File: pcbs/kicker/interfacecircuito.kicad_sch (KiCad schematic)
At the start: 70 parts, among them J1 XT30PW-F, J2 12V, J3 3.3V, J4 BOOST_BOARD, J5 Conn_02x08_Odd_Even, J6 Conn_01x03, Q1 IRFB3077, Q2 IRFB3077, Q3 BC338, U2 IR2101, U3 PC817, U4 LM358, U5 LM324, U6 LM324

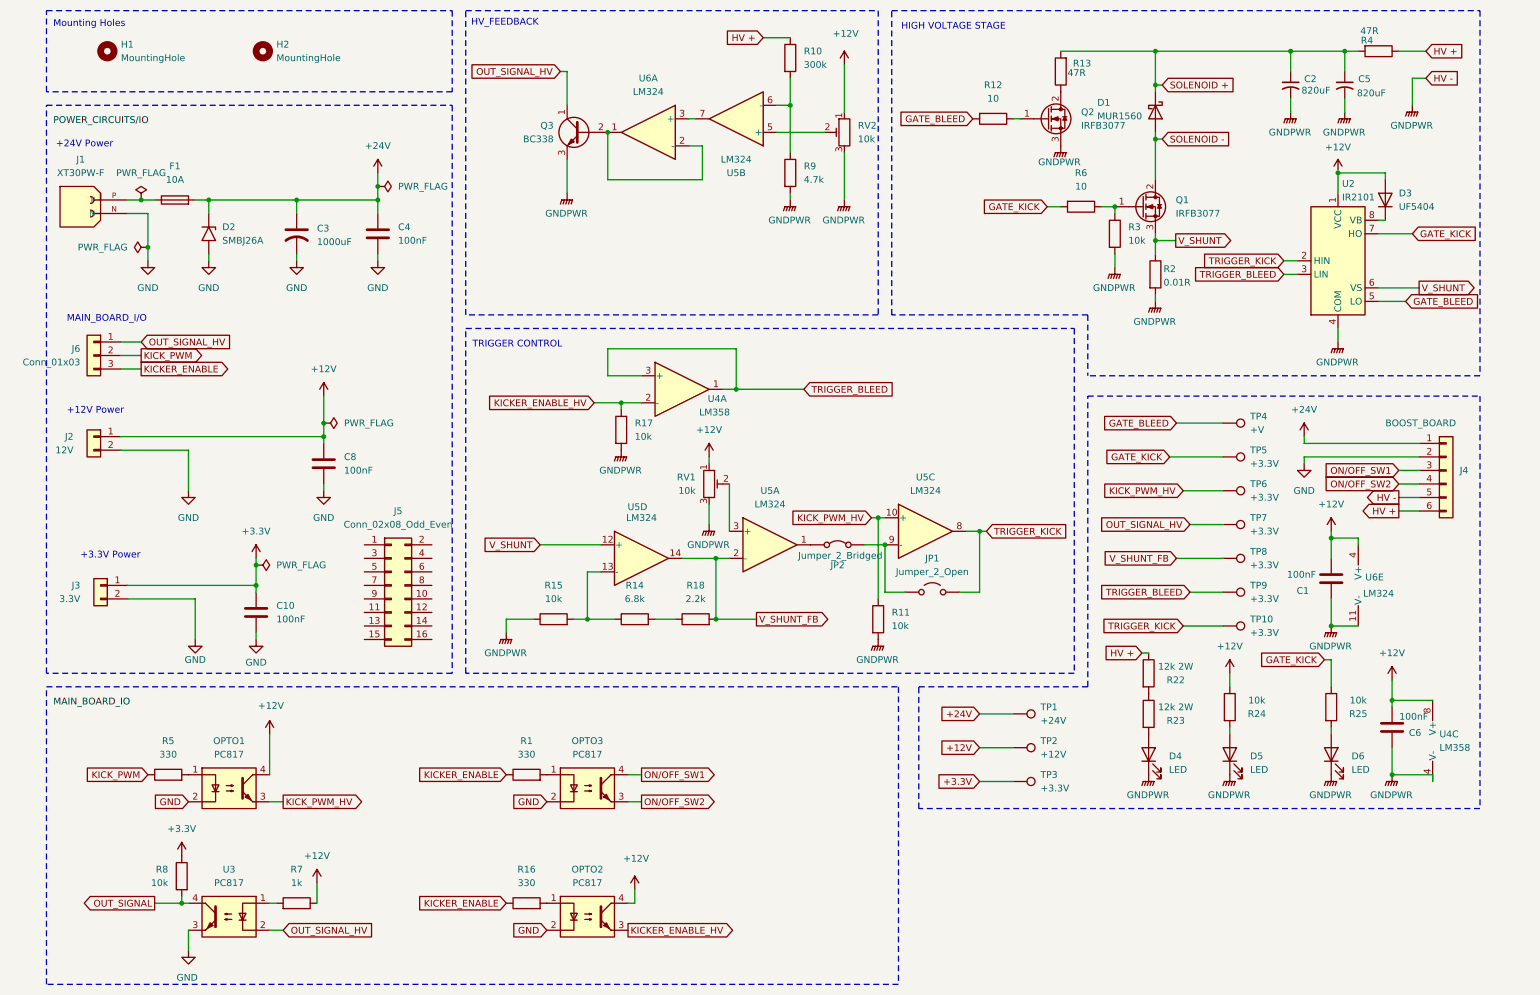
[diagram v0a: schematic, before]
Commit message: Roteamento das trilhas & Footprints
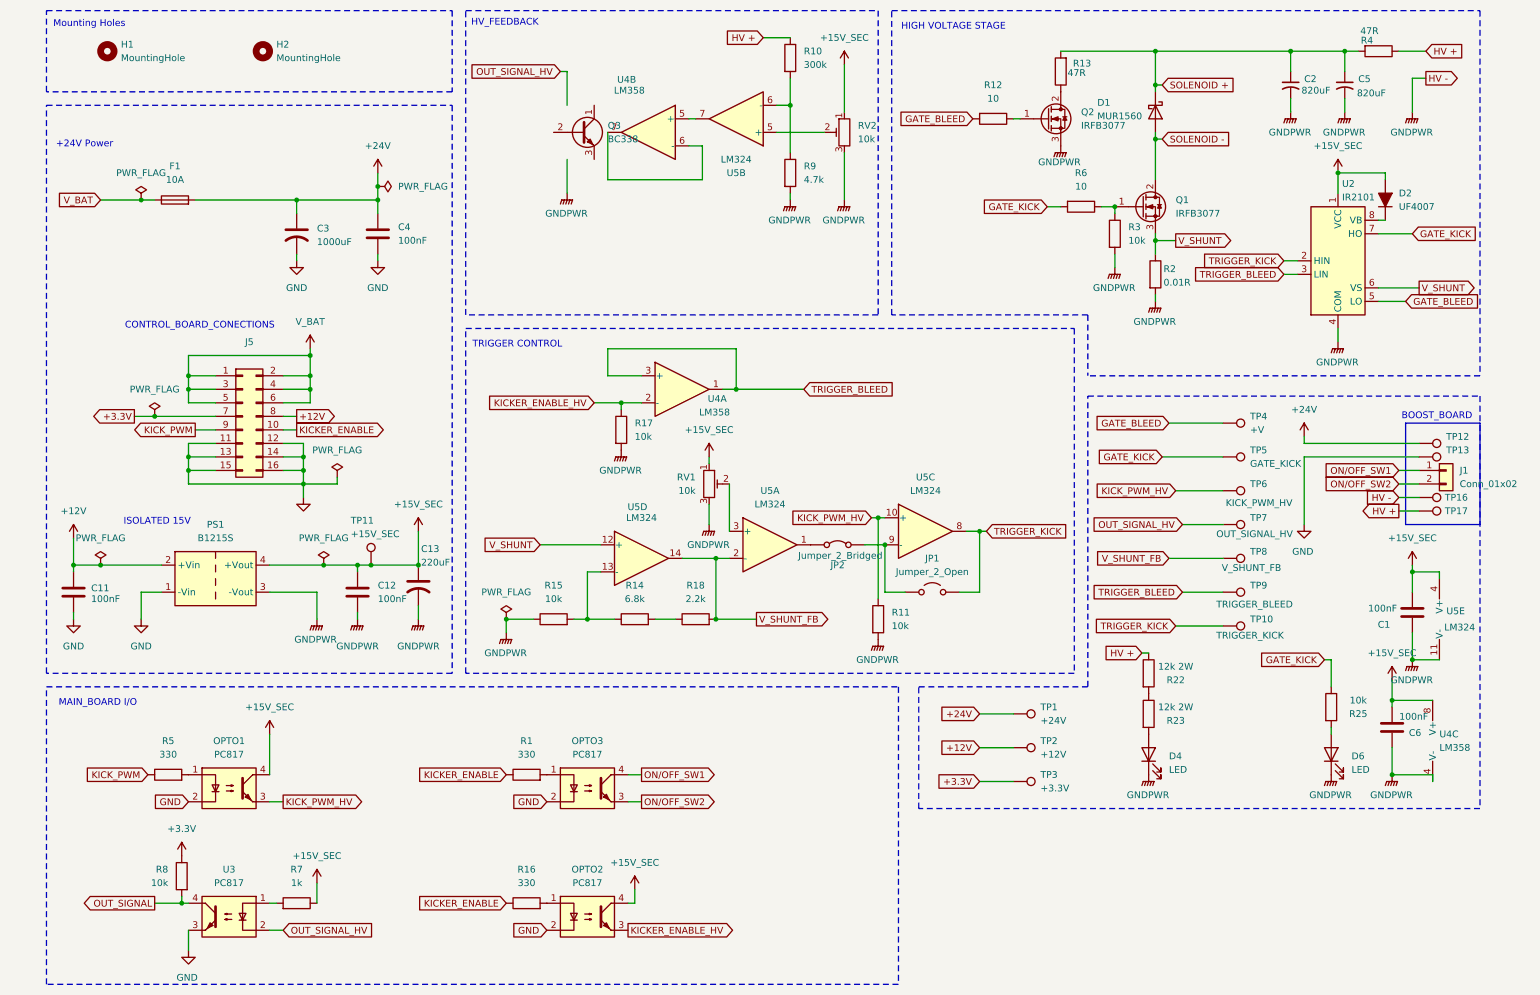
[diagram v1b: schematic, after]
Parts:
- removed C10, C8: 100nF, Capacitor_SMD:C_0805_2012Metric_Pad1.18x1.45mm_HandSolder, symbol Device:C
- removed D2: SMBJ26A, Diode_SMD:D_SMB, symbol Diode:SMAJ26A
- removed D3: UF5404, Diode_THT:D_DO-201AD_P15.24mm_Horizontal, symbol Diode:UF5404
- removed D5: LED, symbol Device:LED
- removed J1: XT30PW-F, oxebots:AMASS_XT30PW-M, symbol oxebots:XT30PW-F
- removed J2: 12V, Connector_JST:JST_PH_S2B-PH-K_1x02_P2.00mm_Horizontal, symbol Connector_Generic:Conn_01x02
- removed J3: 3.3V, Connector_JST:JST_PH_S2B-PH-K_1x02_P2.00mm_Horizontal, symbol Connector_Generic:Conn_01x02
- removed J4: BOOST_BOARD, symbol Connector_Generic:Conn_01x06
- removed J6: Conn_01x03, symbol Connector_Generic:Conn_01x03
- removed R24: 10k, Resistor_SMD:R_2512_6332Metric_Pad1.40x3.35mm_HandSolder, symbol Device:R
- removed unit 1 of U6
- added C11, C12: 100nF, Capacitor_THT:C_Disc_D5.0mm_W2.5mm_P2.50mm, symbol Device:C
- added C13: 220uF, Capacitor_THT:CP_Radial_D8.0mm_P5.00mm, symbol Device:C_US
- added D2: UF4007, PCM_Diode_THT_AKL:D_DO-41_SOD81_P10.16mm_Horizontal, symbol PCM_Diode_AKL:UF4007
- added J1: Conn_01x02, Connector_PinHeader_1.00mm:PinHeader_1x02_P1.00mm_Vertical, symbol Connector_Generic:Conn_01x02
- added PS1: B1215S, oxebots:DC-DC_Converter_BxxxxS_1W, symbol oxebots:Converter_DC-DC_BxxxxS
- added TP11: +15V_SEC, TestPoint:TestPoint_Pad_D1.5mm, symbol Connector:TestPoint
- added TP12: V+, TestPoint:TestPoint_Plated_Hole_D2.0mm, symbol Connector:TestPoint
- added TP13: GND, TestPoint:TestPoint_Plated_Hole_D2.0mm, symbol Connector:TestPoint
- added TP16: HV-, TestPoint:TestPoint_Plated_Hole_D2.0mm, symbol Connector:TestPoint
- added TP17: HV+, TestPoint:TestPoint_Plated_Hole_D2.0mm, symbol Connector:TestPoint
- added unit 2 of U4
- C1, C6: footprint (none) -> Capacitor_THT:C_Disc_D5.0mm_W2.5mm_P2.50mm
- C2, C5: footprint (none) -> Capacitor_THT:C_Radial_D18.0mm_H35.5mm_P7.50mm
- C4: footprint Capacitor_SMD:C_0805_2012Metric_Pad1.18x1.45mm_HandSolder -> Capacitor_THT:C_Disc_D5.0mm_W2.5mm_P2.50mm
- D1: footprint (none) -> Package_TO_SOT_THT:TO-220-2_Vertical
- D4, D6: footprint (none) -> LED_SMD:LED_0805_2012Metric_Pad1.15x1.40mm_HandSolder
- JP1: footprint (none) -> Jumper:SolderJumper-2_P1.3mm_Open_RoundedPad1.0x1.5mm
- JP2: footprint (none) -> Jumper:SolderJumper-2_P1.3mm_Bridged_RoundedPad1.0x1.5mm
- Q1, Q2: footprint (none) -> Package_TO_SOT_THT:TO-220-3_Vertical
- R1, R11, R12, R14, R15, R16, R17, R18, R3, R5, R6, R7, R8, R9: footprint (none) -> Resistor_THT:R_Axial_DIN0207_L6.3mm_D2.5mm_P10.16mm_Horizontal
- R10: footprint (none) -> Resistor_THT:R_Axial_DIN0411_L9.9mm_D3.6mm_P15.24mm_Horizontal
- R13, R4: footprint (none) -> PCM_Resistor_THT_AKL:R_Axial_Power_L25.0mm_W9.0mm_P30.48mm
- R2: footprint (none) -> PCM_Resistor_THT_AKL:R_Axial_DIN0516_L15.5mm_D5.0mm_P20.32mm_Horizontal
- R22, R23: footprint Resistor_SMD:R_2512_6332Metric_Pad1.40x3.35mm_HandSolder -> Resistor_THT:R_Axial_DIN0617_L17.0mm_D6.0mm_P20.32mm_Horizontal
- R25: footprint Resistor_SMD:R_2512_6332Metric_Pad1.40x3.35mm_HandSolder -> Resistor_THT:R_Axial_DIN0207_L6.3mm_D2.5mm_P10.16mm_Horizontal
- RV1, RV2: footprint (none) -> Potentiometer_THT:Potentiometer_Bourns_3296W_Vertical
- TP10: value +3.3V -> TRIGGER_KICK
- TP5: value +3.3V -> GATE_KICK
- TP6: value +3.3V -> KICK_PWM_HV
- TP7: value +3.3V -> OUT_SIGNAL_HV
- TP8: value +3.3V -> V_SHUNT_FB
- TP9: value +3.3V -> TRIGGER_BLEED
- U2, U4: footprint (none) -> Package_SO:SOIC-8_3.9x4.9mm_P1.27mm
- U5: renamed from U6; footprint (none) -> Package_SO:SOIC-14_3.9x8.7mm_P1.27mm
- U5: footprint (none) -> Package_SO:SOIC-14_3.9x8.7mm_P1.27mm
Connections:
- net +12V: now also J5.8 (Pin_8), C11.1, PS1.2 (+Vin); no longer C1.1, C6.1, OPTO1.4, OPTO2.4, R7.1, RV1.1, RV2.1, U2.1 (VCC), U4.8 (V+), U5.4 (V+)
- net +24V: now also TP12.1
- net +3.3V: now also J5.7 (Pin_7)
- net GND: now also J5.11 (Pin_11), J5.12 (Pin_12), J5.13 (Pin_13), J5.14 (Pin_14), J5.15 (Pin_15), J5.16 (Pin_16), C11.2, PS1.1 (-Vin), TP13.1
- net GNDPWR: now also C12.2, C13.2, PS1.3 (-Vout), TP16.1; no longer Q3.3 (E)
- net HV +: now also TP17.1
- net KICKER_ENABLE: now also J5.10 (Pin_10)
- net KICK_PWM: now also J5.9 (Pin_9)
- net ON/OFF_SW1: now also J1.1 (Pin_1)
- net ON/OFF_SW2: now also J1.2 (Pin_2)
- net OUT_SIGNAL_HV: no longer Q3.1 (C)
- net at U2.8 (VB): now also D2.1 (K)
- net V_BAT: now reaches F1.1
- net V_BAT: now also J5.1 (Pin_1), J5.2 (Pin_2), J5.3 (Pin_3), J5.4 (Pin_4), J5.5 (Pin_5), J5.6 (Pin_6)
- net at U5.7: now also U4.5 (+)
- new net: U4.6 (-), U4.7
- new net +15V_SEC: C1.1, C12.1, C13.1, C6.1, D2.2 (A), OPTO1.4, OPTO2.4, PS1.4 (+Vout), R7.1, RV1.1, RV2.1, TP11.1, U2.1 (VCC), U4.8 (V+), U5.4 (V+)
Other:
- note added: "BOOST_BOARD"
- note added: "CONTROL_BOARD_CONECTIONS"
- note added: "ISOLATED 15V"
- note added: "MAIN_BOARD I/O"
- note removed: "+12V Power"
- note removed: "+3.3V Power"
- note removed: "MAIN_BOARD_I/O"
- moved on the sheet: C1, J5, Q3, U5E

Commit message: Resolução de Warnings do esquemático, substituição de conectores on/off e conector de solenoide
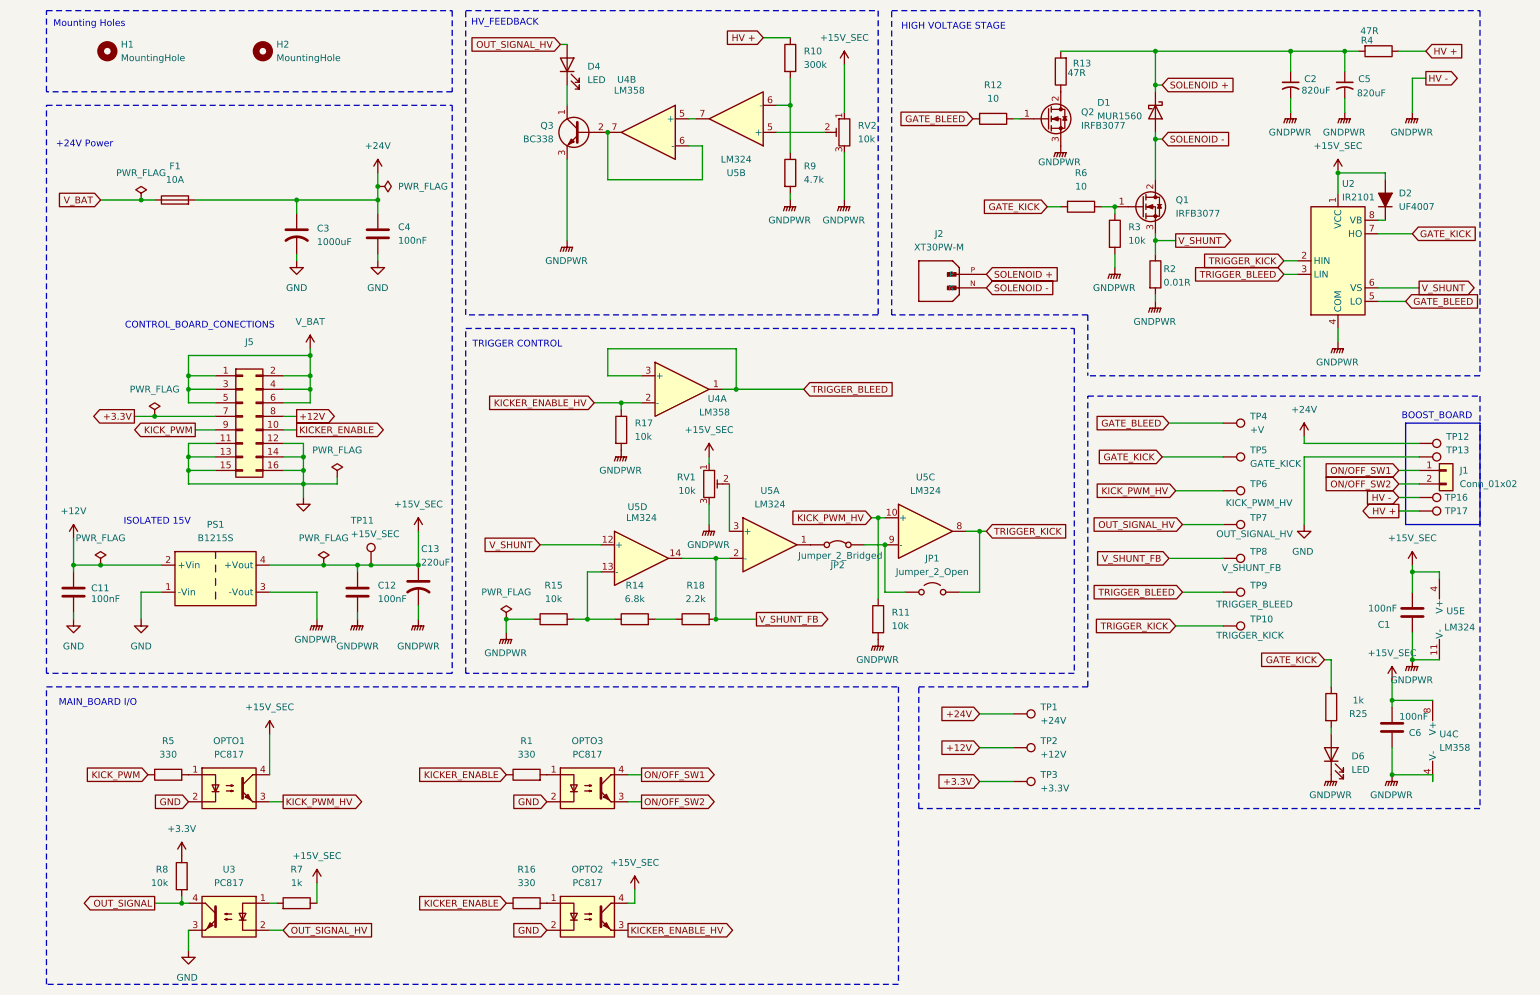
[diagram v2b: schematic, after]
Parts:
- removed R22, R23: 12k 2W, Resistor_THT:R_Axial_DIN0617_L17.0mm_D6.0mm_P20.32mm_Horizontal, symbol Device:R
- added J2: XT30PW-M, oxebots:AMASS_XT30PW-M, symbol oxebots:XT30PW-M
- D4, D6: footprint LED_SMD:LED_0805_2012Metric_Pad1.15x1.40mm_HandSolder -> LED_THT:LED_D5.0mm
- J1: footprint Connector_PinHeader_1.00mm:PinHeader_1x02_P1.00mm_Vertical -> Connector_JST:JST_EH_B2B-EH-A_1x02_P2.50mm_Vertical
- R25: value 10k -> 1k
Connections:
- net GNDPWR: now also Q3.3 (E); no longer D4.1 (K)
- net OUT_SIGNAL_HV: now also D4.2 (A)
- net SOLENOID +: now also J2.P
- net SOLENOID -: now also J2.N
- net at Q3.1 (C): now also D4.1 (K)
- net at Q3.2 (B): now also U4.6 (-), U4.7
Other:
- moved on the sheet: Q3

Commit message: Resolução de EDR Mudança nas trilhas de 24V mudança do footprint dos capacitores bulk
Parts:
- C2, C5: footprint Capacitor_THT:C_Radial_D18.0mm_H35.5mm_P7.50mm -> Capacitor_THT:CP_Radial_D30.0mm_P10.00mm_SnapIn
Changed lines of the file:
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@@
 	)
 	(junction
-		(at 66.04 118.11)
+		(at 222.25 45.72)
 		(diameter 0)
 		(color 0 0 0 0)
@@
 	(wire
 		(pts
+			(xy 222.25 45.72) (xy 231.14 45.72)
+		)
+		(stroke
+			(width 0)
+			(type default)
+		)
+	)
+	(wire
+		(pts
 			(xy 62.23 95.25) (xy 58.42 95.25)
 		)
@@
 	(wire
 		(pts
-			(xy 66.04 118.11) (xy 74.93 118.11)
+			(xy 55.88 118.11) (xy 74.93 118.11)
 		)
 		(stroke
@@
 	(wire
 		(pts
-			(xy 55.88 118.11) (xy 66.04 118.11)
-		)
-		(stroke
-			(width 0)
-			(type default)
-		)
-	)
-	(wire
-		(pts
 			(xy 274.32 157.48) (xy 266.7 157.48)
 		)
@@
 			)
 		)
-		(property "Footprint" "Capacitor_THT:C_Radial_D18.0mm_H35.5mm_P7.50mm"
+		(property "Footprint" "Capacitor_THT:CP_Radial_D30.0mm_P10.00mm_SnapIn"
 			(at 257.81 27.94 0)
 			(hide yes)
@@
 			)
 		)
-		(property "Footprint" "Capacitor_THT:C_Radial_D18.0mm_H35.5mm_P7.50mm"
+		(property "Footprint" "Capacitor_THT:CP_Radial_D30.0mm_P10.00mm_SnapIn"
 			(at 247.65 27.94 0)
 			(hide yes)
@@
 	)
 	(symbol
+		(lib_id "power:PWR_FLAG")
+		(at 222.25 21.59 0)
+		(unit 1)
+		(body_style 1)
+		(exclude_from_sim no)
+		(in_bom yes)
+		(on_board yes)
+		(in_pos_files yes)
+		(dnp no)
+		(fields_autoplaced yes)
+		(property "Reference" "#FLG010"
+			(at 222.25 19.685 0)
+			(hide yes)
+			(show_name no)
+			(do_not_autoplace no)
+			(effects
+				(font
+					(size 1.27 1.27)
+				)
+			)
+		)
+		(property "Value" "PWR_FLAG"
+			(at 222.25 16.51 0)
+			(show_name no)
+			(do_not_autoplace no)
+			(effects
+				(font
+					(size 1.27 1.27)
+				)
+			)
+		)
+		(property "Footprint" ""
+			(at 222.25 21.59 0)
+			(hide yes)
+			(show_name no)
+			(do_not_autoplace no)
+			(effects
+				(font
+					(size 1.27 1.27)
+				)
+			)
+		)
+		(property "Datasheet" "~"
+			(at 222.25 21.59 0)
+			(hide yes)
+			(show_name no)
+			(do_not_autoplace no)
+			(effects
+				(font
+					(size 1.27 1.27)
+				)
+			)
+		)
+		(property "Description" "Special symbol for telling ERC where power comes from"
+			(at 222.25 21.59 0)
+			(hide yes)
+			(show_name no)
+			(do_not_autoplace no)
+			(effects
+				(font
+					(size 1.27 1.27)
+				)
+			)
+		)
+		(pin "1"
+		)
+		(instances
+			(project "interfacecircuito"
+				(path "/21d6ebf1-8438-4874-a5b6-238c3ba91f04"
+					(reference "#FLG010")
+					(unit 1)
+				)
+			)
+		)
+	)
+	(symbol
 		(lib_id "Connector:TestPoint")
 		(at 234.95 129.54 270)
@@
 	)
 	(symbol
-		(lib_id "power:PWR_FLAG")
-		(at 66.04 118.11 0)
-		(unit 1)
-		(body_style 1)
-		(exclude_from_sim no)
-		(in_bom yes)
-		(on_board yes)
-		(in_pos_files yes)
-		(dnp no)
-		(fields_autoplaced yes)
-		(property "Reference" "#FLG07"
-			(at 66.04 116.205 0)
-			(hide yes)
-			(show_name no)
-			(do_not_autoplace no)
-			(effects
-				(font
-					(size 1.27 1.27)
-				)
-			)
-		)
-		(property "Value" "PWR_FLAG"
-			(at 66.04 113.03 0)
-			(show_name no)
-			(do_not_autoplace no)
-			(effects
-				(font
-					(size 1.27 1.27)
-				)
-			)
-		)
-		(property "Footprint" ""
-			(at 66.04 118.11 0)
-			(hide yes)
-			(show_name no)
-			(do_not_autoplace no)
-			(effects
-				(font
-					(size 1.27 1.27)
-				)
-			)
-		)
-		(property "Datasheet" "~"
-			(at 66.04 118.11 0)
-			(hide yes)
-			(show_name no)
-			(do_not_autoplace no)
-			(effects
-				(font
-					(size 1.27 1.27)
-				)
-			)
-		)
-		(property "Description" "Special symbol for telling ERC where power comes from"
-			(at 66.04 118.11 0)
-			(hide yes)
-			(show_name no)
-			(do_not_autoplace no)
-			(effects
-				(font
-					(size 1.27 1.27)
-				)
-			)
-		)
-		(pin "1"
-		)
-		(instances
-			(project "interfacecircuito"
-				(path "/21d6ebf1-8438-4874-a5b6-238c3ba91f04"
-					(reference "#FLG07")
-					(unit 1)
-				)
-			)
-		)
-	)
-	(symbol
 		(lib_id "Device:R")
 		(at 109.22 128.27 90)
@@
 					(unit 1)
 				)
+			)
+		)
+	)
+	(symbol
+		(lib_id "power:PWR_FLAG")
+		(at 231.14 45.72 0)
+		(unit 1)
+		(body_style 1)
+		(exclude_from_sim no)
+		(in_bom yes)
+		(on_board yes)
+		(in_pos_files yes)
+		(dnp no)
+		(fields_autoplaced yes)
+		(property "Reference" "#FLG011"
+			(at 231.14 43.815 0)
+			(hide yes)
+			(show_name no)
+			(do_not_autoplace no)
+			(effects
+				(font
+					(size 1.27 1.27)
+				)
+			)
+		)
+		(property "Value" "PWR_FLAG"
+			(at 231.14 40.64 0)
+			(show_name no)
+			(do_not_autoplace no)
+			(effects
+				(font
+					(size 1.27 1.27)
+				)
+			)
+		)
+		(property "Footprint" ""
+			(at 231.14 45.72 0)
+			(hide yes)
+			(show_name no)
+			(do_not_autoplace no)
+			(effects
+				(font
+					(size 1.27 1.27)
+				)
+			)
+		)
+		(property "Datasheet" "~"
+			(at 231.14 45.72 0)
+			(hide yes)
+			(show_name no)
+			(do_not_autoplace no)
+			(effects
+				(font
+					(size 1.27 1.27)
+				)
+			)
+		)
+		(property "Description" "Special symbol for telling ERC where power comes from"
+			(at 231.14 45.72 0)
+			(hide yes)
+			(show_name no)
+			(do_not_autoplace no)
+			(effects
+				(font
+					(size 1.27 1.27)
+				)
+			)
+		)
+		(pin "1"
+		)
+		(instances
+			(project "interfacecircuito"
+				(path "/21d6ebf1-8438-4874-a5b6-238c3ba91f04"
+					(reference "#FLG011")
+					(unit 1)
+				)
